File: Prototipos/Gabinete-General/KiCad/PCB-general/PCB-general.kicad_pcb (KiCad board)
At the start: 2 copper layers, 50 x 100 mm, 18 parts, among them J1 Conn_01x02, J2 Conn_01x02, J3 TFT Display, J4 PCIe X4, M3_BL MountingHole_3.2mm_M3, M3_BR MountingHole_3.2mm_M3, M3_TL MountingHole_3.2mm_M3, M3_TR MountingHole_3.2mm_M3, SW1 RotaryEncoder_Switch, U1 ESP32-S3-DevKitC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

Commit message: Rediseñar PCB gabinete central
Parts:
- C1: value 100 nF -> 330 nF
- C3: value 100nF -> 1uF
- J4: footprint Proyecto_Final:PCIE_x4_Gabinete_NSH -> ProyectoFinal:PCIE_x4_Gabinete_NSH
- moved C1 78.2 mm to (169.7, 140.6), turned to 180 degrees
- moved SW1 5.00 mm to (198.0, 121.9)
- moved C4 4.32 mm to (203.3, 111.2)
- moved R1 4.32 mm to (198.3, 117.7)
- moved R3 4.32 mm to (198.3, 113.5)
- moved R2 4.32 mm to (198.3, 115.6)
- moved U1 3.90 mm to (167.4, 83.9)
- moved J3 1.50 mm to (161.1, 134.8)
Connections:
- C1 pad 1: PGND -> 5Vdc
- C1 pad 2: AGND -> GND
- C2 pad 2: PGND -> GND
- C3 pad 2: PGND -> GND
- C4 pad 1: AGND -> GND
- J1 pad 2: PGND -> GND
- J3 pad 2: AGND -> GND
- J4 pad 2: PGND -> GND
- J4 pad 7: AGND -> GND
- SW1 pad 2: AGND -> GND
- SW1 pad 5: AGND -> GND
- U1 pad 22: AGND -> GND
- U1 pad 23: AGND -> GND
- U1 pad 24: AGND -> GND
- U1 pad 44: AGND -> GND
- U2 pad 2: PGND -> GND
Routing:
- net GND: track 0.00 -> 403.1 mm, vias 0 -> 10
- net AGND: track 177.6 -> 0.00 mm, vias 6 -> 0
- net PGND: track 70.7 -> 0.00 mm
- net PCIe_MODULE_IDENT: track 51.7 -> 94.4 mm
- net 3.3Vdc: track 145.5 -> 181.8 mm, vias 0 -> 2
- net 5Vdc: track 152.7 -> 175.1 mm, vias 2 -> 4
- net PCIe_S16: track 25.2 -> 6.08 mm
- net PCIe_S9: track 42.5 -> 60.1 mm, vias 0 -> 2
- net PCIe_HP_Power: track 65.8 -> 80.7 mm
- net 12Vdc: track 65.0 -> 53.5 mm
- net PCIe_S12: track 24.9 -> 35.6 mm
- net PCIe_S1: track 38.2 -> 48.9 mm
- net PCIe_S3: track 39.3 -> 49.6 mm
- net PCIe_S5: track 40.3 -> 49.9 mm
- net PCIe_S14: track 19.2 -> 28.4 mm
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- added copper zone on B.Cu, net GND
- removed copper zone on B.Cu, net AGND
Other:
- board size 50 x 100 mm -> 53.5 x 100 mm

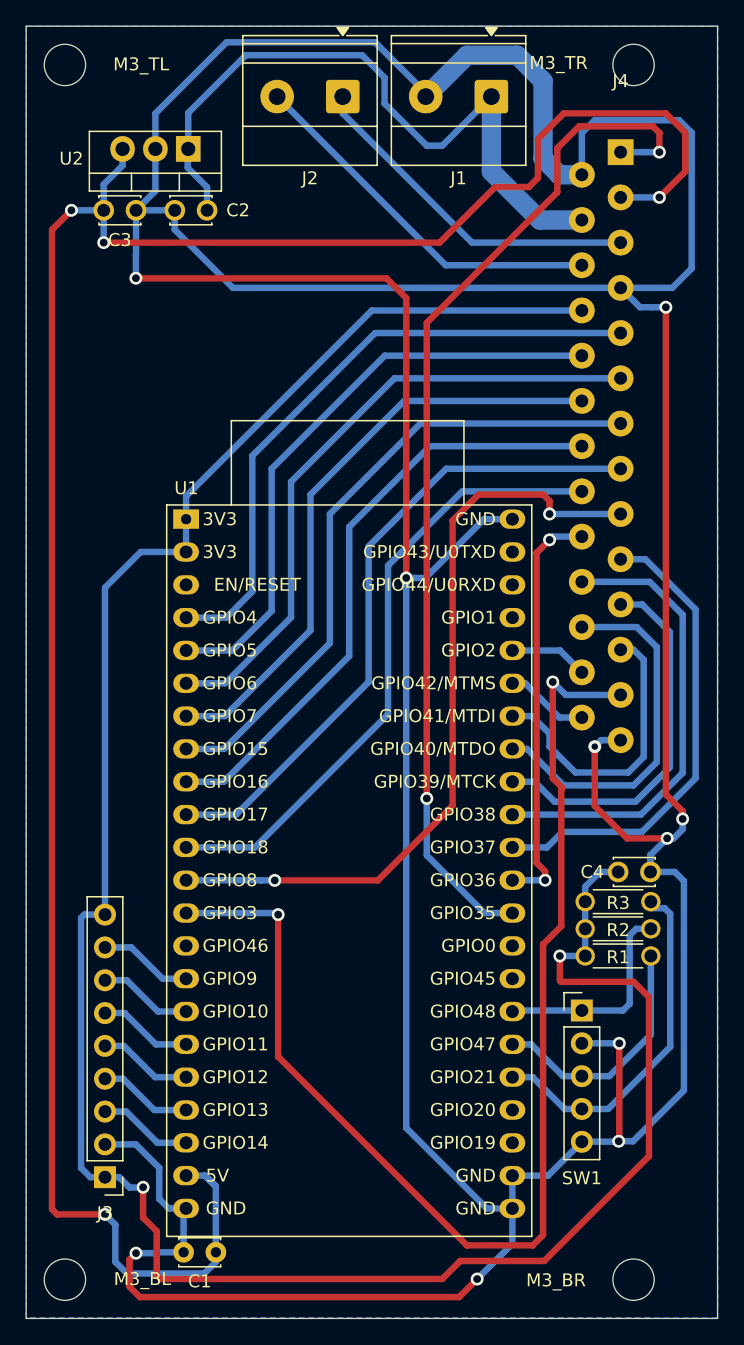
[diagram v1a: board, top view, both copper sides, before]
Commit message: Agrandar tamaño pad vias
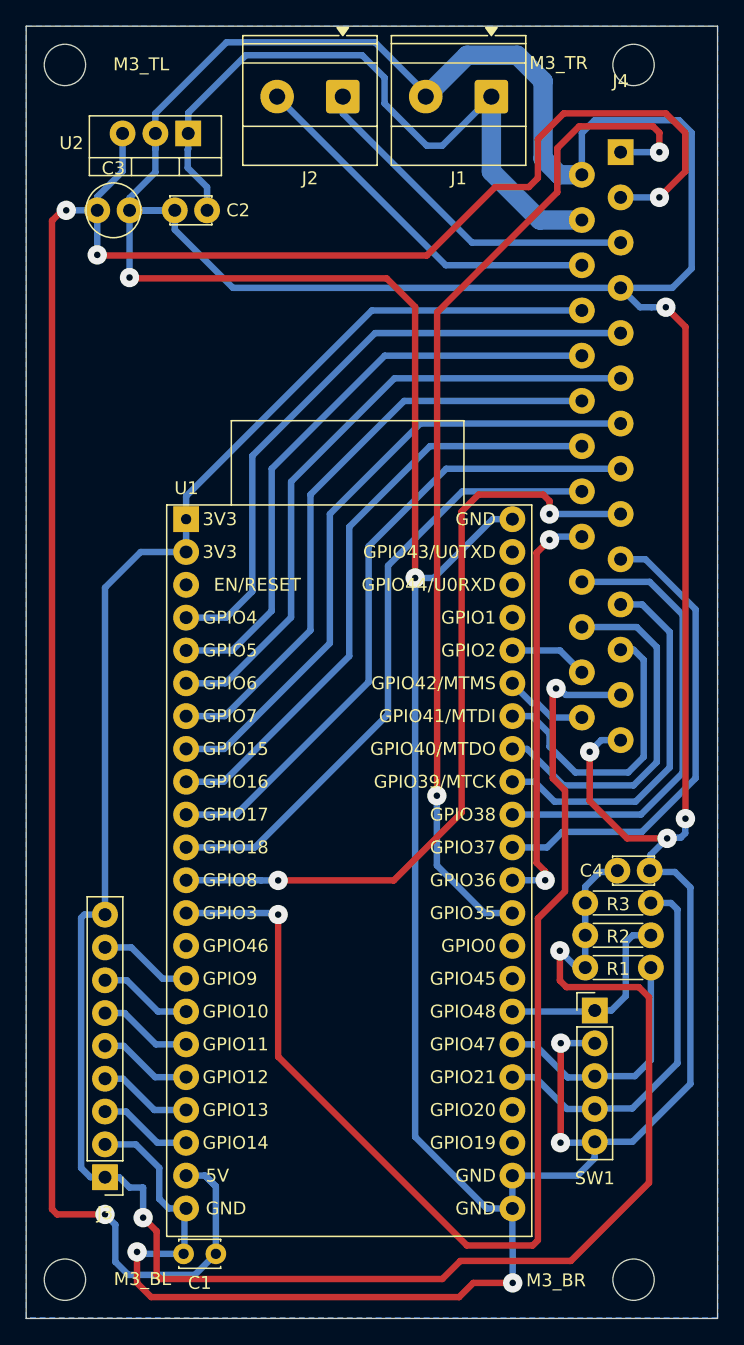
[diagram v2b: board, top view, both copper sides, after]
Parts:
- C3: footprint Capacitor_THT:C_Disc_D3.0mm_W2.0mm_P2.50mm -> Capacitor_THT:C_Radial_D4.0mm_H7.0mm_P1.50mm
- moved U2 1.20 mm to (167.5, 54.0)
- moved SW1 1.00 mm to (199.0, 121.9)
- moved R1 0.90 mm to (198.3, 118.6)
- moved R2 0.50 mm to (198.3, 116.1)
- moved C1 0.12 mm to (169.7, 140.8)
- moved C4 0.12 mm to (203.2, 111.1)
- moved R3 0.10 mm to (198.3, 113.6)
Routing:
- net GND: track 403.1 -> 411.4 mm
- net 3.3Vdc: track 181.8 -> 184.7 mm
- net 5Vdc: track 175.1 -> 177.9 mm
- net ROTARY_SW: track 27.2 -> 29.4 mm
- net ROTARY_CLK: track 16.5 -> 15.7 mm
- net PCIe_S9: track 60.1 -> 60.9 mm
- net PCIe_MODULE_IDENT: track 94.4 -> 93.8 mm
- net PCIe_HP_Power: track 80.7 -> 80.1 mm
